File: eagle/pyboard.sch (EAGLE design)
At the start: 58 parts, among them IC1 STM32F405RGT, Q1 8MHz, Q2 32.768kHz, U1 MCP1802

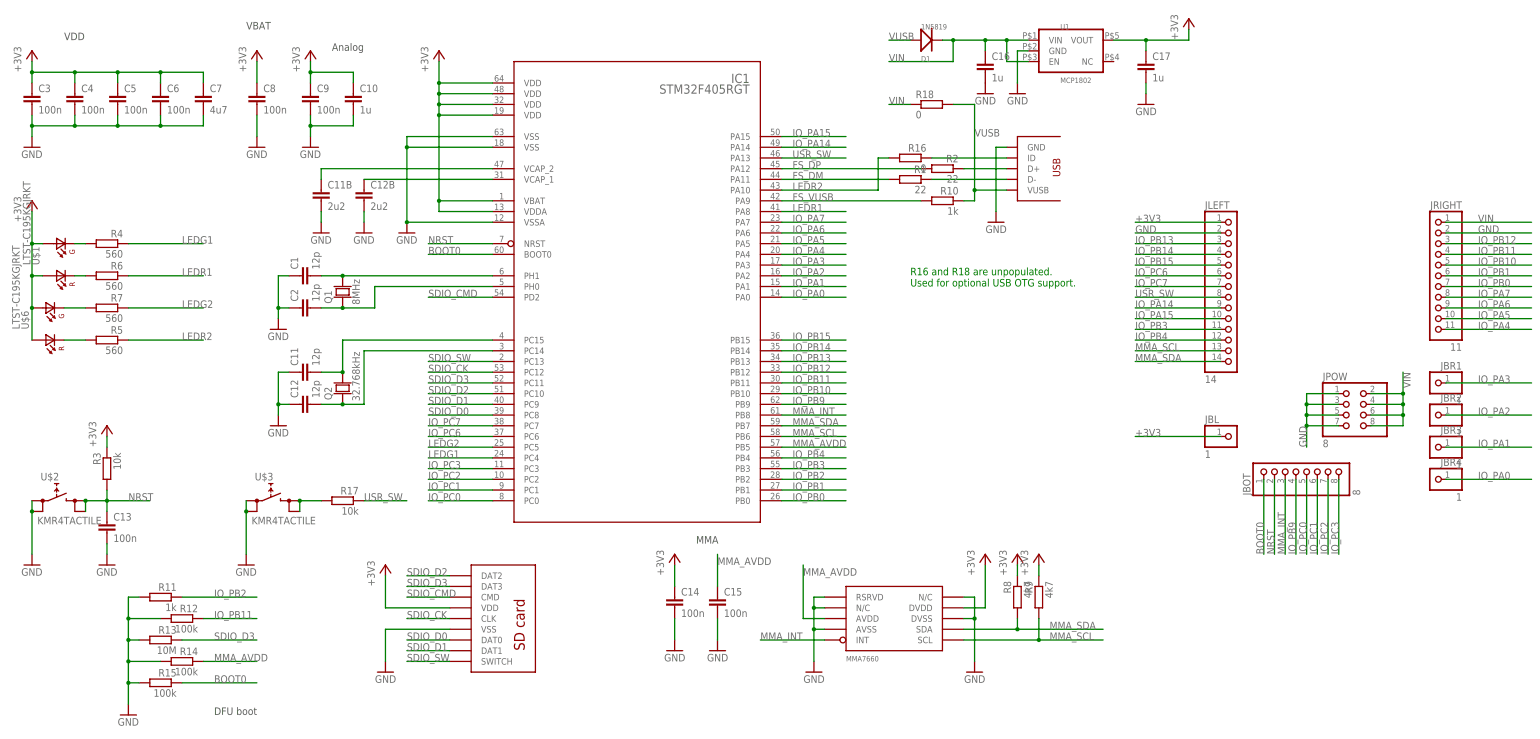
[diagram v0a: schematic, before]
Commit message: updated pyboard to more closely resemble the newer v10 boards for which eagle files aren't available yet
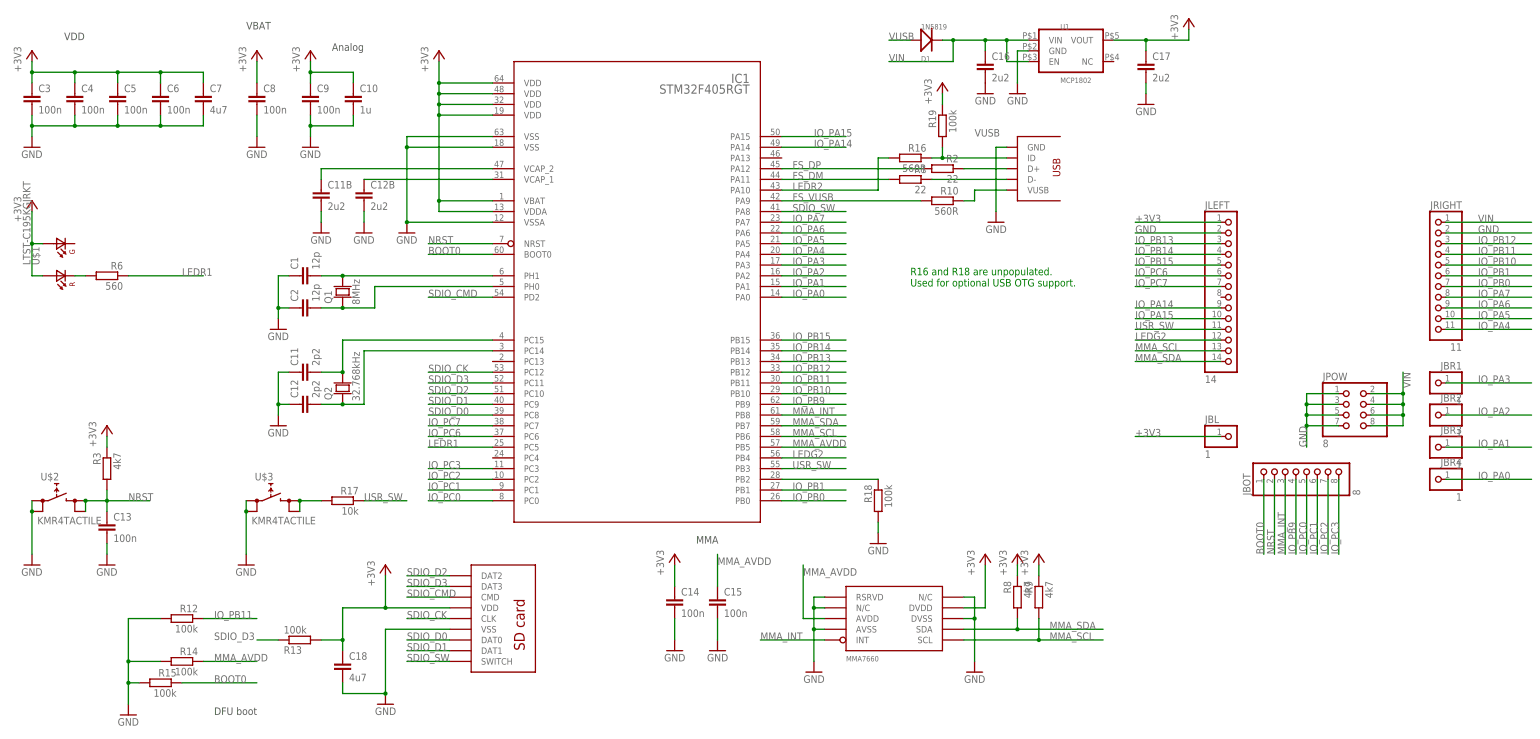
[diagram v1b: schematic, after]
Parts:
- removed R11: 1k, rcl:R-EU_R0603
- removed R4, R5, R7: 560, rcl:R-EU_R0603
- removed U$6: LTST-C195KGJRKT, pyboard:LTST-C195KGJRKT
- added C18: 4u7, rcl:C-EUC0603
- added R19: 100k, rcl:R-EU_R0603
- C11, C12: value 12p -> 2p2
- C16, C17: value 1u -> 2u2
- R10: value 1k -> 560R
- R13: value 10M -> 100k
- R16: value 0 -> 560R
- R18: value 0 -> 100k; device rcl:R-EU_R0805 -> rcl:R-EU_R0603
- R3: value 10k -> 4k7
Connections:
- removed net IO_PB2: IC1.PB2, R11.1
- removed net IO_PB3: IC1.PB3, JLEFT.11
- removed net IO_PB4: IC1.PB4, JLEFT.12
- removed net LEDG1: IC1.PC4, R4.1
- removed net N$11: R4.2, U$1.K1
- removed net N$12: R5.2, U$6.K2
- removed net N$14: R7.2, U$6.K1
- new net N$8: IC1.PB2, R18.1
- net +3V3: now also C18.1, R13.2, R19.1; no longer U$6.A1, U$6.A2
- net GND: now also C18.2, R18.2; no longer R11.2, R13.2
- net LEDG2: now also IC1.PB4, JLEFT.12; no longer IC1.PC5, R7.1
- net LEDR1: now also IC1.PC5; no longer IC1.PA8
- net LEDR2: no longer R5.1
- net N$7: now also R19.2
- net SDIO_SW: now also IC1.PA8; no longer IC1.PC13
- net USR_SW: now also IC1.PB3, JLEFT.11; no longer IC1.PA13, JLEFT.8
- net VIN: no longer R18.1
- net VUSB: no longer R18.2
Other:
- moved on the sheet: R13, R18

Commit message: old computer changes, double check
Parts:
- C1, C2: PARTNO (none) -> CL10C120JB8NNNC
- C10: PARTNO (none) -> YNA18B2C0G105M
- C11, C12: PARTNO (none) -> CL10C2R2CB8NNNC
- C11B, C12B, C16, C17: PARTNO (none) -> LMK107B7225KA-T
- C13, C14, C15, C3, C4, C5, C6, C8, C9: PARTNO (none) -> C0603C104J4RACTU
- C18, C7: PARTNO (none) -> CL10B475KQ8NQNC
- D1: PARTNO (none) -> 1N5819HW-7-F
- IC1: PARTNO (none) -> STM32F405RGT6
- JBL, JBOT, JBR1, JBR2, JBR3, JBR4, JLEFT, JPOW, JRIGHT: BOM (none) -> EXCLUDE
- Q1: PARTNO (none) -> AA-8.000MALV-T
- Q2: PARTNO (none) -> ABS07-120-32.768KHZ-T
- R1, R2: PARTNO (none) -> MCR03ERTJ220
- R10, R16, R6: PARTNO (none) -> RC0603FR-07560RL
- R12, R13, R14, R15, R18, R19: PARTNO (none) -> RC0603JR-07100KL
- R17: PARTNO (none) -> RC0603JR-0710KL
- R3, R8, R9: PARTNO (none) -> RC0603JR-074K7L
- U$1: PARTNO (none) -> LTST-C195KGJRKT
- U$2, U$3: PARTNO (none) -> KMR442G LFS
- U$4: PARTNO (none) -> 1050270001
- U$5: PARTNO (none) -> MMA7660FCR1
- U$7: PARTNO (none) -> ZX62D-AB-5P8
- U1: PARTNO (none) -> MCP1802T-3302I/OT
